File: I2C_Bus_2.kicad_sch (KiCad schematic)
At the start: 10 parts, among them U10 SAM-M10Q, U4 BMI088, U9 MS5611-01BA

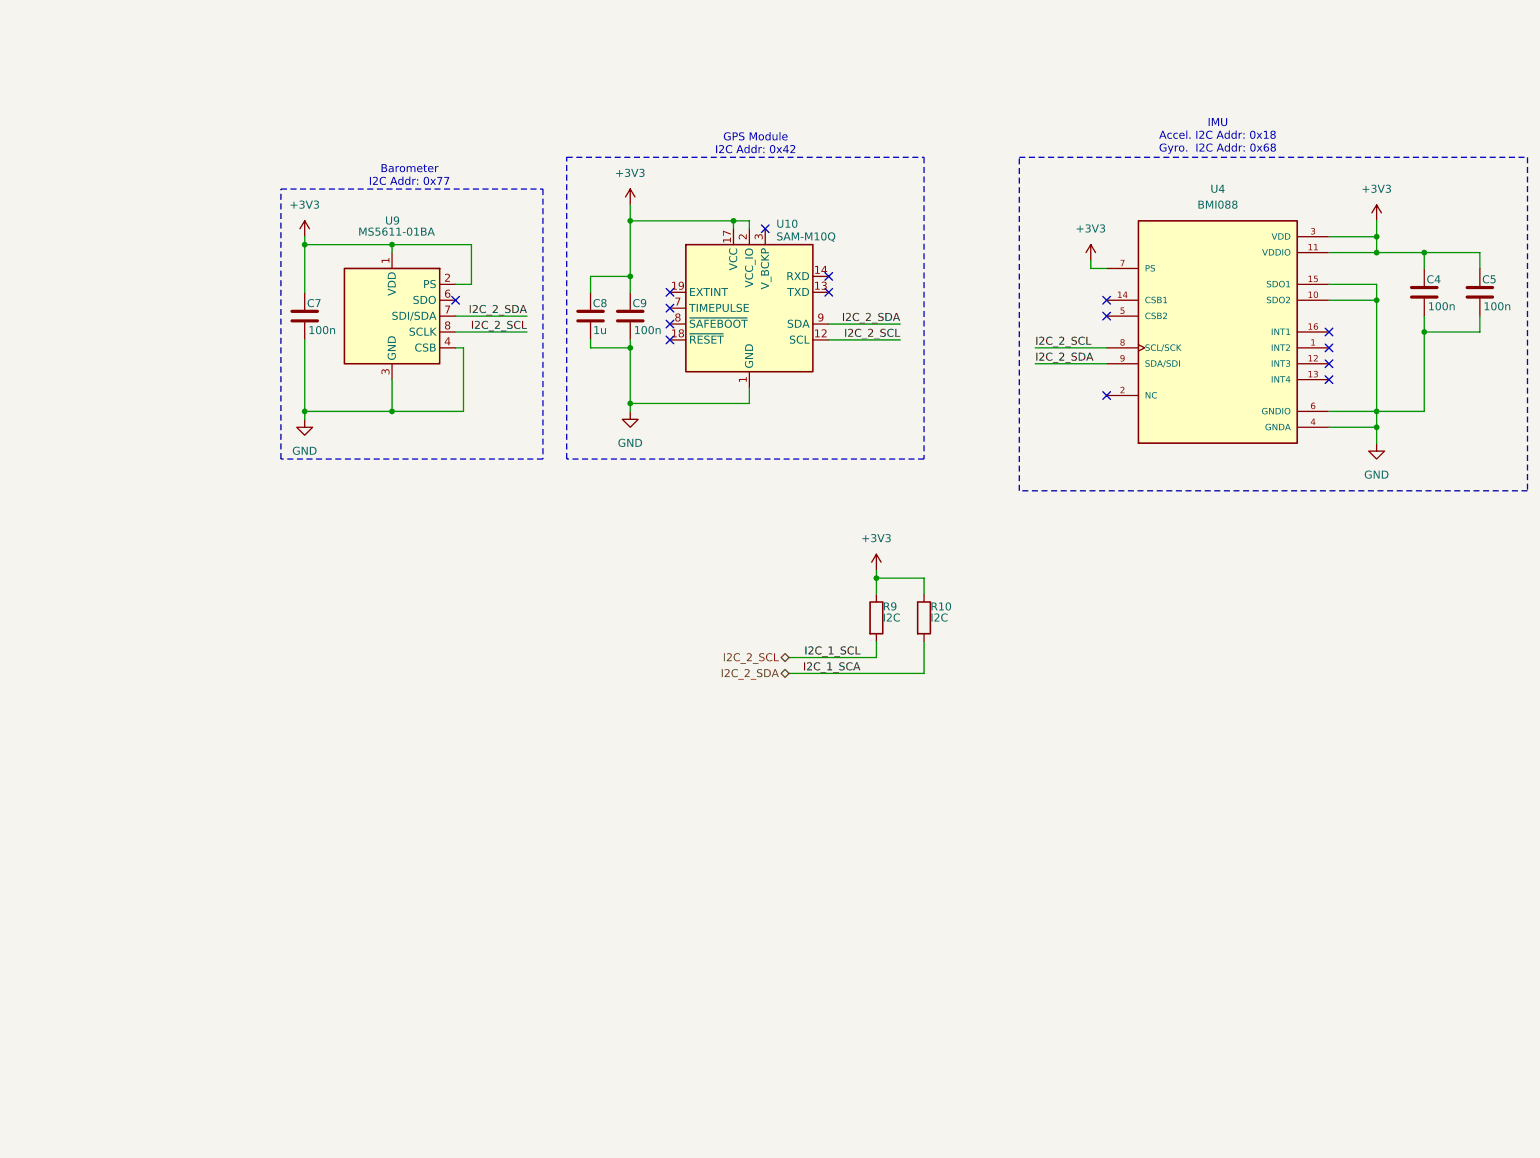
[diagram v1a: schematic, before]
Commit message: Added buttons, LEDs, TPs, and Miku
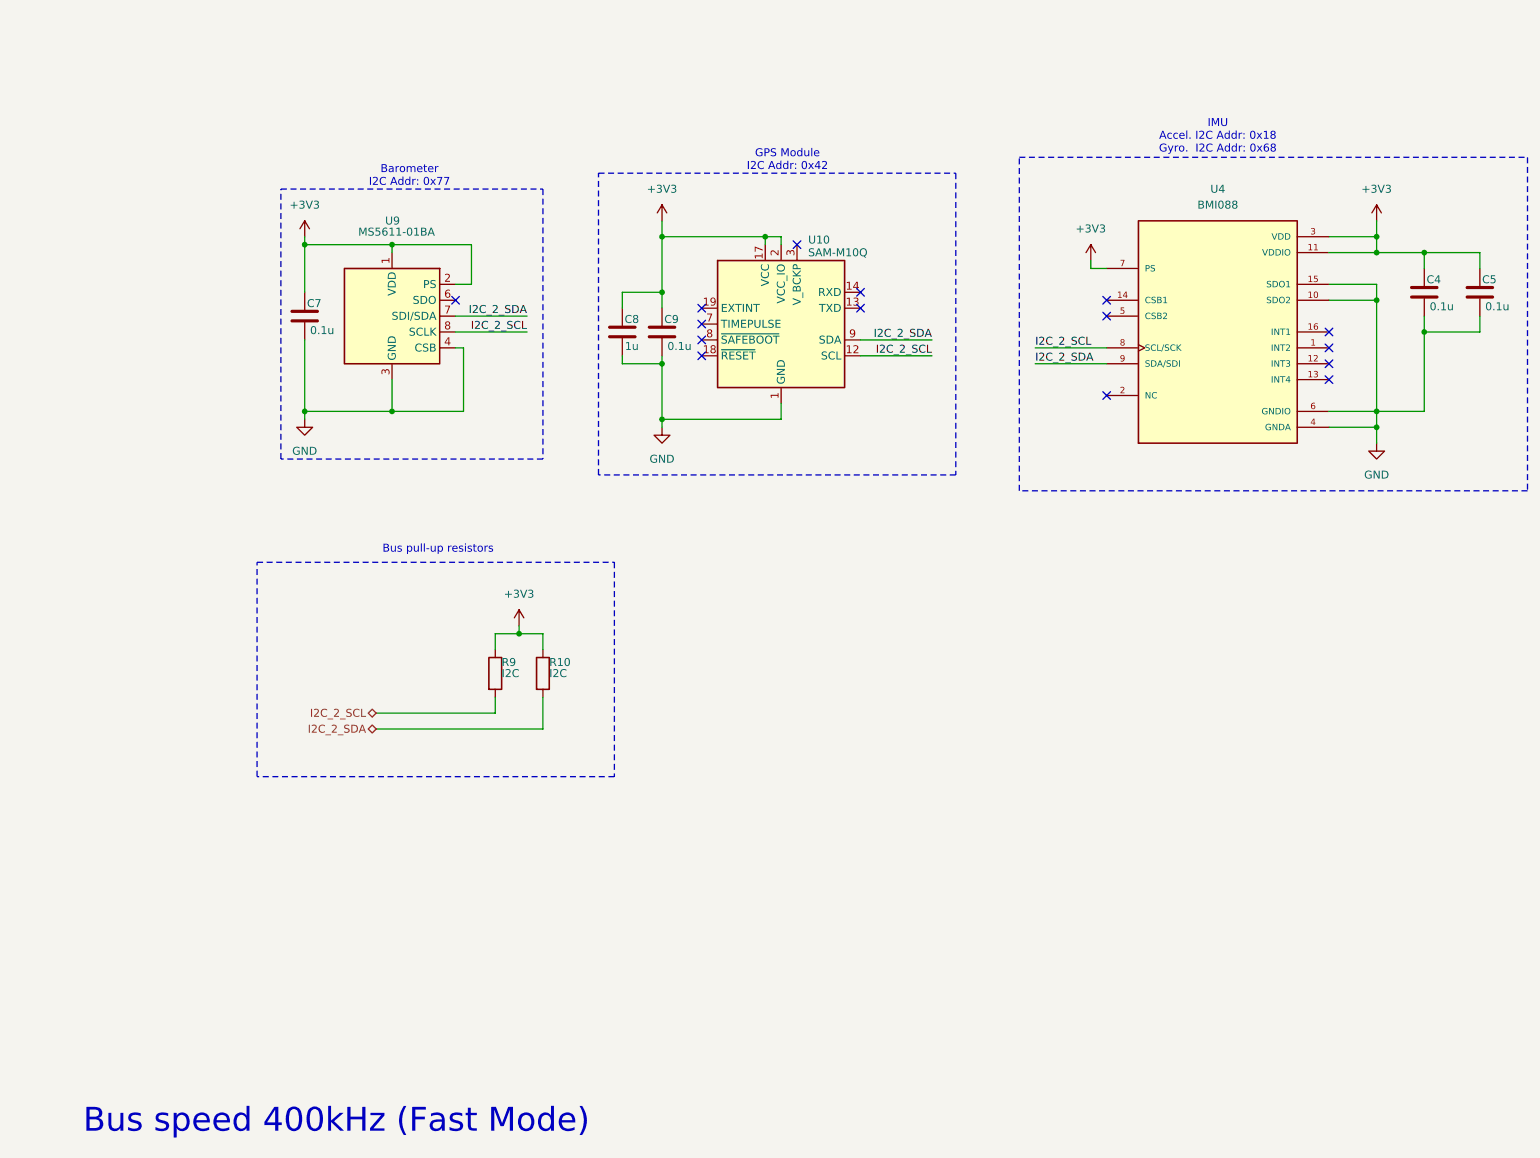
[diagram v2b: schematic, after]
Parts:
- C4, C5, C7, C9: value 100n -> 0.1u
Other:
- note added: "Bus pull-up resistors"
- note added: "Bus speed 400kHz (Fast Mode)"
- moved on the sheet: C8, C9, R10, R9, U10

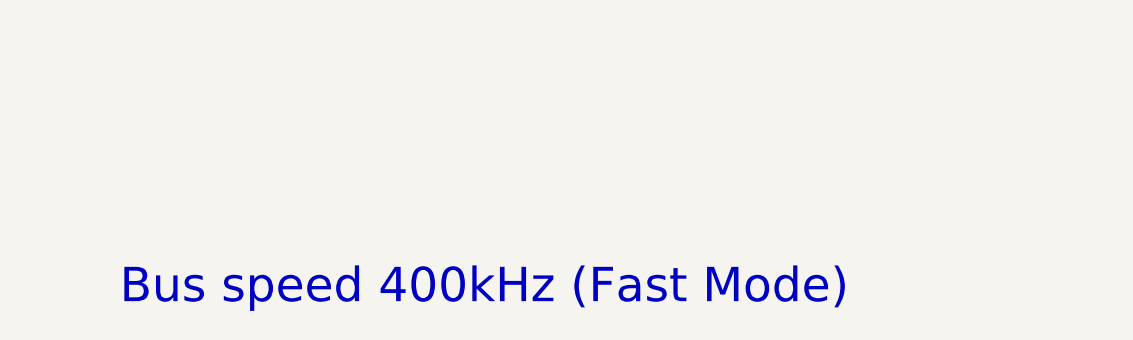
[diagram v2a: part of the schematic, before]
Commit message: Tentatively finished schematic
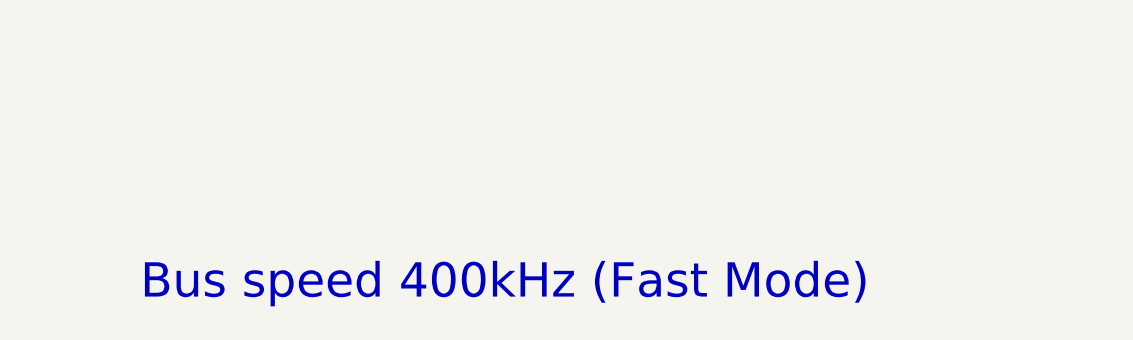
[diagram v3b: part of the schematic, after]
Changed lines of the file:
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@@
 	(text "Bus speed 400kHz (Fast Mode)\n"
 		(exclude_from_sim no)
-		(at 59.69 192.278 0)
+		(at 61.976 191.77 0)
 		(effects
 			(font

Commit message: Added I2C resistor values
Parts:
- R10, R9: value I2C -> 1k
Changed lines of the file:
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@@
 			)
 		)
-		(property "Value" "I2C"
+		(property "Value" "1k"
 			(at 86.106 120.65 0)
 			(effects
@@
 			)
 		)
-		(property "Value" "I2C"
+		(property "Value" "1k"
 			(at 93.726 120.65 0)
 			(effects

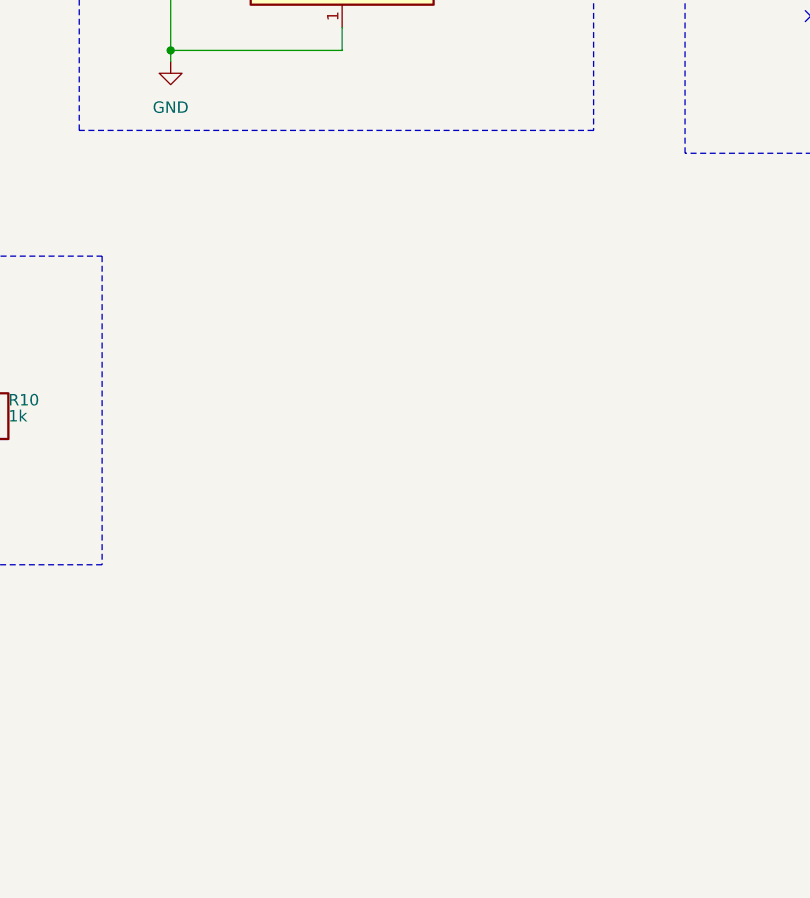
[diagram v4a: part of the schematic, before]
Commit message: Moved LIS3MDL to FM bus
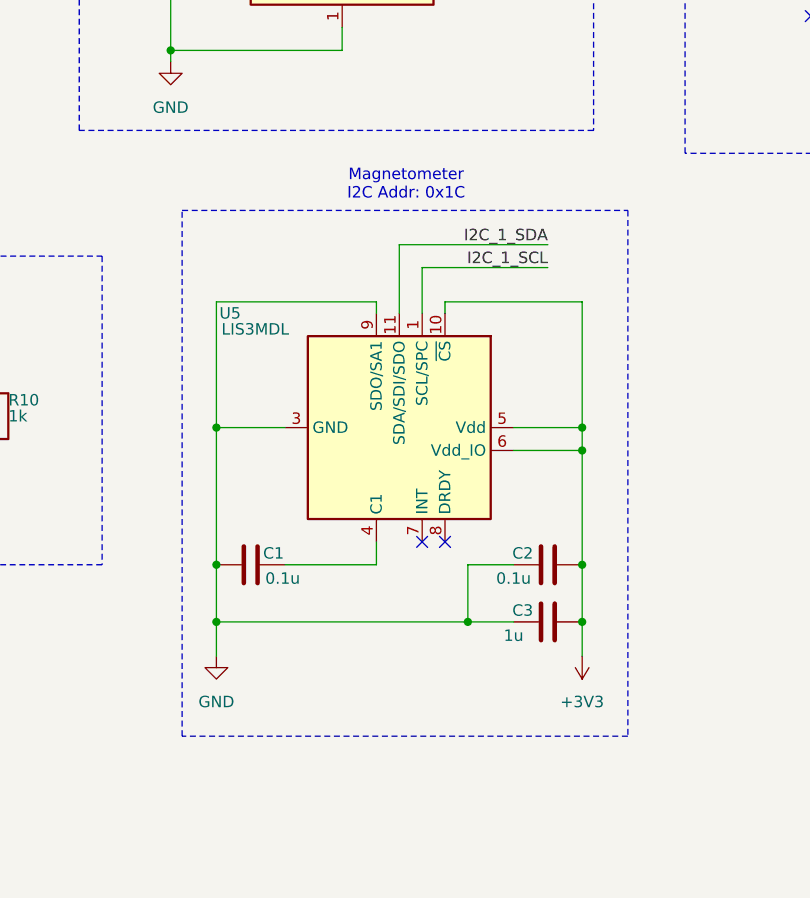
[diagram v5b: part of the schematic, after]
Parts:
- added C1, C2: 0.1u, Capacitor_SMD:C_0603_1608Metric, symbol Device:C
- added C3: 1u, Capacitor_SMD:C_0603_1608Metric, symbol Device:C
- added U5: LIS3MDL, Package_LGA:LGA-12_2x2mm_P0.5mm, symbol Sensor_Magnetic:LIS3MDL
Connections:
- net +3V3: now also C2.2, C3.2, U5.10 (~{CS}), U5.5 (Vdd), U5.6 (Vdd_IO)
- net GND: now also C1.1, C2.1, C3.1, U5.12 (GND), U5.2 (GND), U5.3 (GND), U5.9 (SDO/SA1)
- new net: C1.2, U5.4 (C1)
- new net I2C_1_SCL: U5.1 (SCL/SPC)
- new net I2C_1_SDA: U5.11 (SDA/SDI/SDO)
- no-connect marks 15 -> 17
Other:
- note added: "Magnetometer I2C Addr: 0x1C"

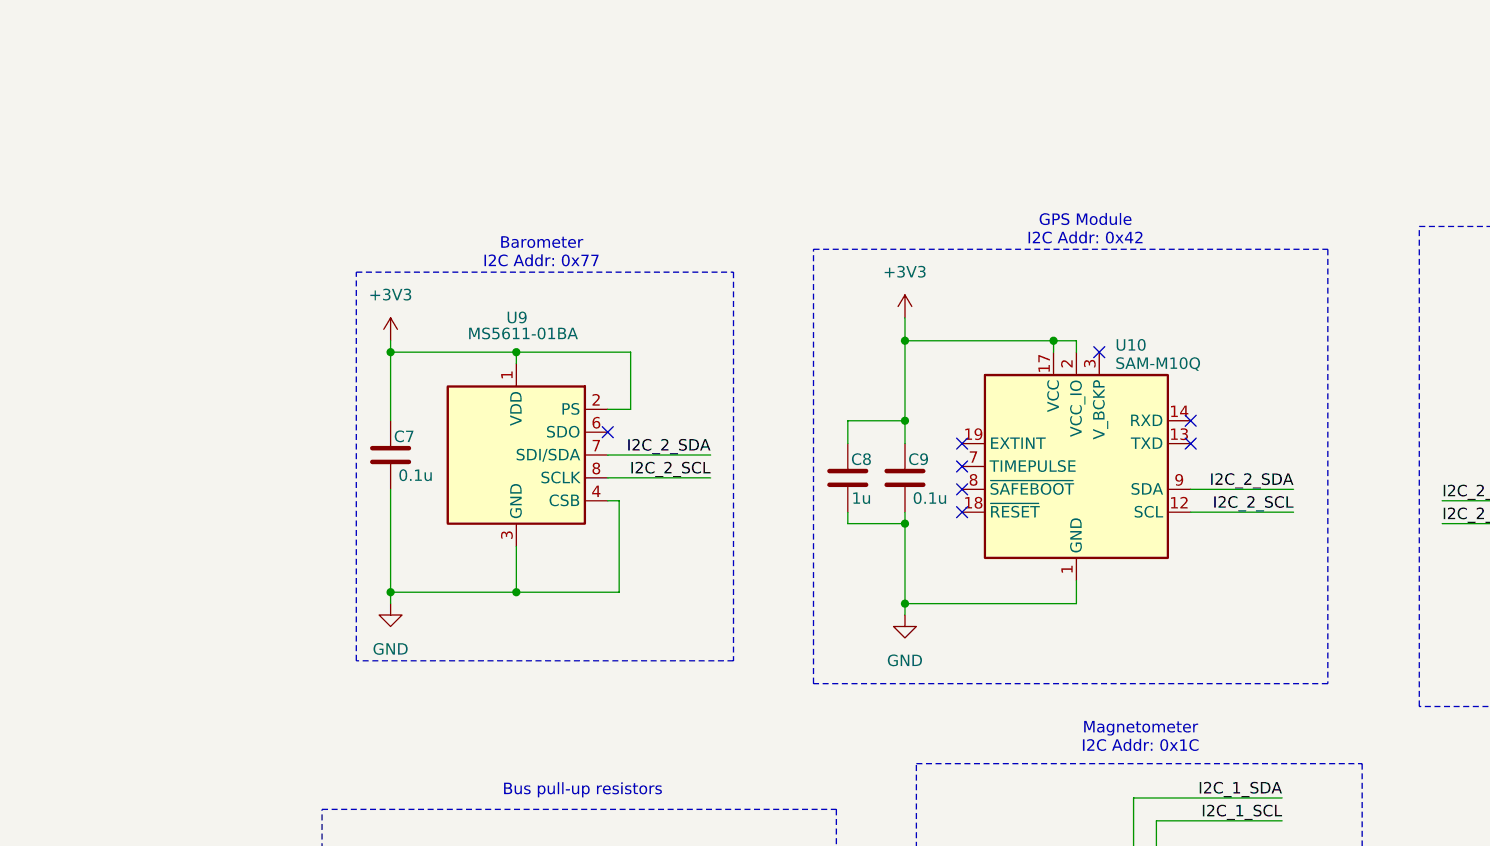
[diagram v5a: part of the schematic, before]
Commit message: Changed out GPS module
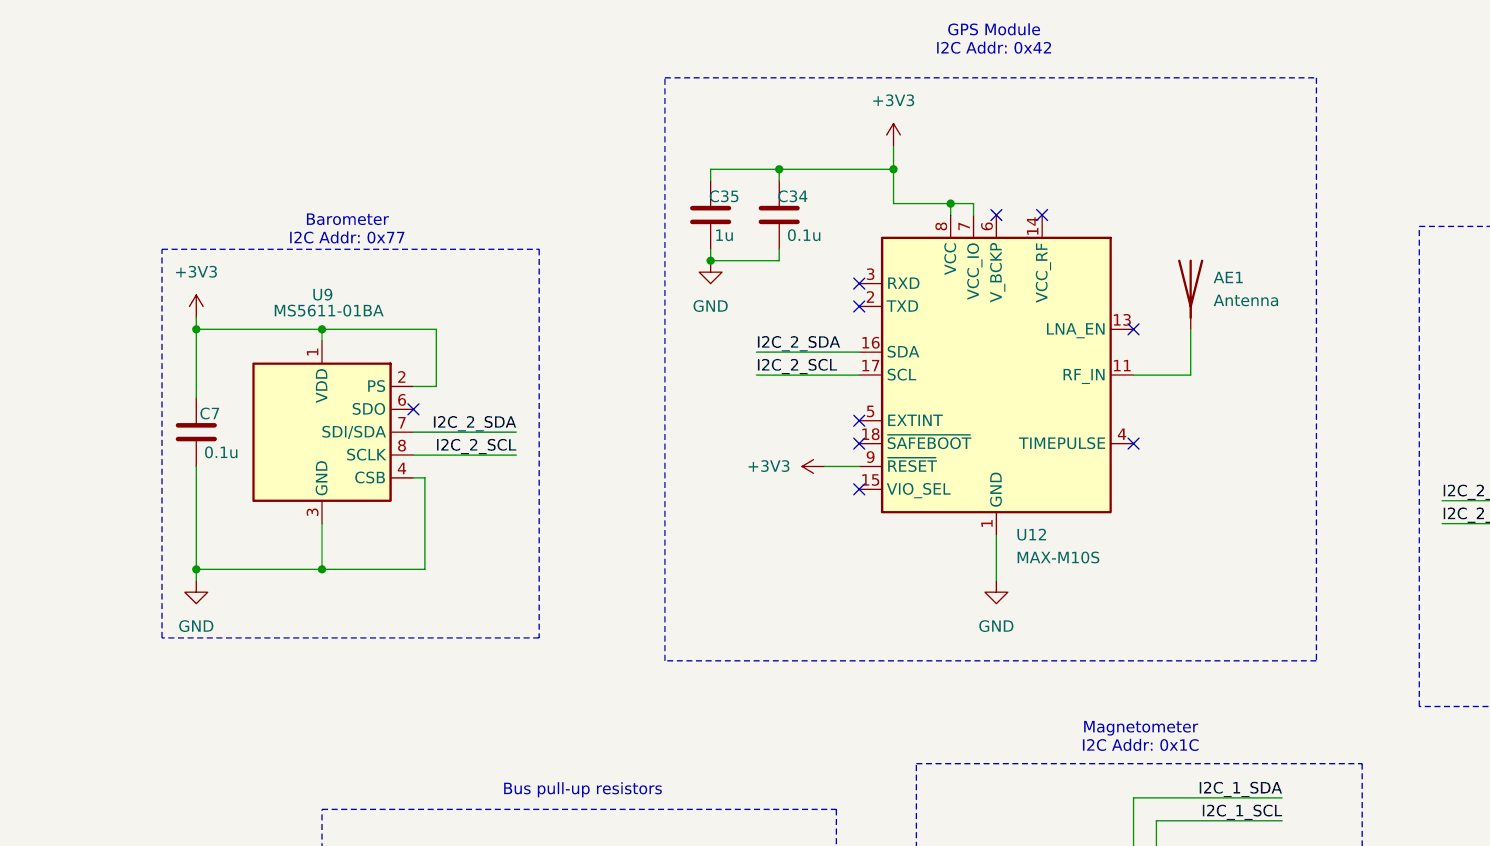
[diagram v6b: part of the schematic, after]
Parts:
- removed C8: 1u, Capacitor_SMD:C_0603_1608Metric, symbol Device:C
- removed C9: 0.1u, Capacitor_SMD:C_0603_1608Metric, symbol Device:C
- removed U10: SAM-M10Q, RF_GPS:ublox_SAM-M8Q, symbol RF_GPS:SAM-M8Q
- added AE1: Antenna, Connector_Coaxial:U.FL_Hirose_U.FL-R-SMT-1_Vertical, symbol Device:Antenna
- added C34: 0.1u, Capacitor_SMD:C_0603_1608Metric, symbol Device:C
- added C35: 1u, Capacitor_SMD:C_0603_1608Metric, symbol Device:C
- added U12: MAX-M10S, RF_GPS:ublox_MAX, symbol RF_GPS:MAX-M10S
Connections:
- net +3V3: now also C34.2, C35.2, U12.7 (VCC_IO), U12.8 (VCC), U12.9 (~{RESET})
- net GND: now also C34.1, C35.1, U12.1 (GND), U12.10 (GND), U12.12 (GND)
- net I2C_2_SCL: now also U12.17 (SCL)
- net I2C_2_SDA: now also U12.16 (SDA)
- new net: AE1.1 (A), U12.11 (RF_IN)
- no-connect marks 17 -> 19
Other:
- moved on the sheet: C7, U9

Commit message: Added 3D model for MAX-M10S and adjusted footprint
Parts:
- U12: footprint RF_GPS:ublox_MAX -> LRI_partlib:ublox_MAX
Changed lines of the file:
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@@
 			)
 		)
-		(property "Footprint" "RF_GPS:ublox_MAX"
+		(property "Footprint" "LRI_partlib:ublox_MAX"
 			(at 132.08 71.12 0)
 			(effects

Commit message: WIP layout/route
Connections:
- net I2C_1_SCL is gone; now on net I2C_2_SCL: U5.1 (SCL/SPC)
- net I2C_1_SDA is gone; now on net I2C_2_SDA: U5.11 (SDA/SDI/SDO)
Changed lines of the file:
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@@
 		)
 	)
-	(label "I2C_1_SDA"
+	(label "I2C_2_SDA"
 		(at 153.67 101.6 180)
 		(fields_autoplaced yes)
@@
 		)
 	)
-	(label "I2C_1_SCL"
+	(label "I2C_2_SCL"
 		(at 153.67 104.14 180)
 		(fields_autoplaced yes)
